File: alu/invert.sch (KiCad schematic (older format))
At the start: 16 parts

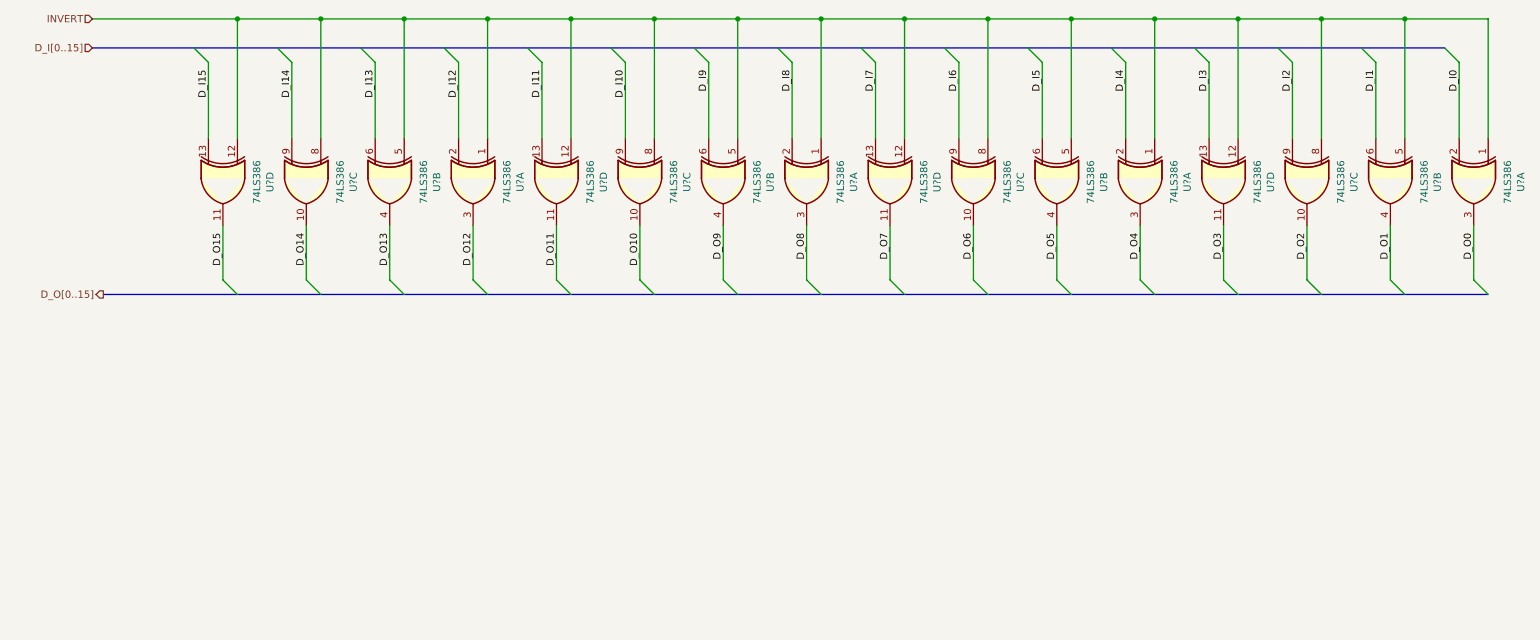
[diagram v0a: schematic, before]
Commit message: alu routed first iteration
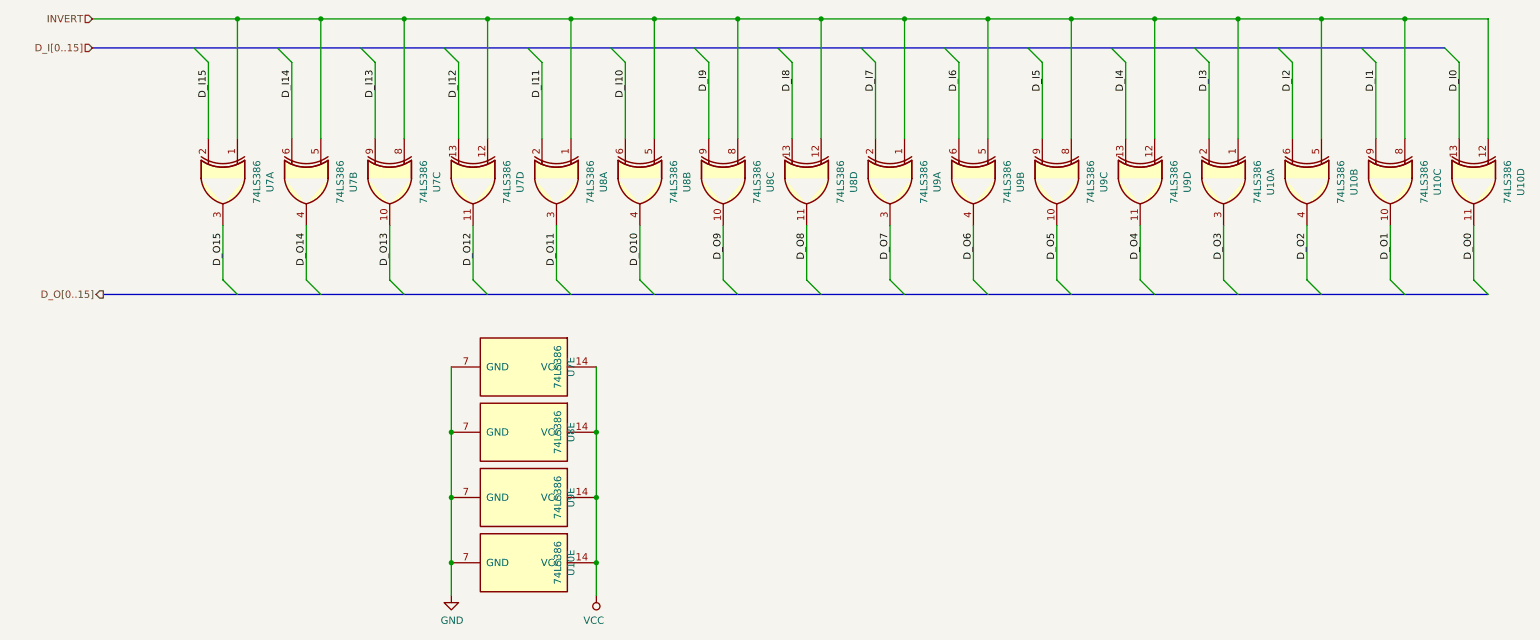
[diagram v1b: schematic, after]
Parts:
- added unit 5 of U10
- added unit 5 of U7
- added unit 5 of U8
- added unit 5 of U9
- U10, U7, U8, U9: renamed from U?; footprint (none) -> Package_DIP:DIP-14_W7.62mm_LongPads
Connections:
- net D_I0: now also U10.13; no longer U10.2
- net D_I1: now also U10.9; no longer U10.6
- net D_I10: now also U8.6; no longer U8.9
- net D_I11: now also U8.2; no longer U8.13
- net D_I12: now also U7.13; no longer U7.2
- net D_I13: now also U7.9; no longer U7.6
- net D_I14: now also U7.6; no longer U7.9
- net D_I15: now also U7.2; no longer U7.13
- net D_I2: now also U10.6; no longer U10.9
- net D_I3: now also U10.2; no longer U10.13
- net D_I4: now also U9.13; no longer U9.2
- net D_I5: now also U9.9; no longer U9.6
- net D_I6: now also U9.6; no longer U9.9
- net D_I7: now also U9.2; no longer U9.13
- net D_I8: now also U8.13; no longer U8.2
- net D_I9: now also U8.9; no longer U8.6
- net D_O0: now also U10.11; no longer U10.3
- net D_O1: now also U10.10; no longer U10.4
- net D_O10: now also U8.4; no longer U8.10
- net D_O11: now also U8.3; no longer U8.11
- net D_O12: now also U7.11; no longer U7.3
- net D_O13: now also U7.10; no longer U7.4
- net D_O14: now also U7.4; no longer U7.10
- net D_O15: now also U7.3; no longer U7.11
- net D_O2: now also U10.4; no longer U10.10
- net D_O3: now also U10.3; no longer U10.11
- net D_O4: now also U9.11; no longer U9.3
- net D_O5: now also U9.10; no longer U9.4
- net D_O6: now also U9.4; no longer U9.10
- net D_O7: now also U9.3; no longer U9.11
- net D_O8: now also U8.11; no longer U8.3
- net D_O9: now also U8.10; no longer U8.4
- net INVERT: now also U10.1, U10.12, U10.5, U10.8, U7.1, U7.12, U7.5, U7.8, U8.1, U8.12, U8.5, U8.8, U9.1, U9.12, U9.5, U9.8; no longer U10.1, U10.12, U10.5, U10.8, U7.1, U7.12, U7.5, U7.8, U8.1, U8.12, U8.5, U8.8, U9.1, U9.12, U9.5, U9.8
- new net GND: U10.7 (GND), U7.7 (GND), U8.7 (GND), U9.7 (GND)
- new net VCC: U10.14 (VCC), U7.14 (VCC), U8.14 (VCC), U9.14 (VCC)

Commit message: Commit uncomitted changes. no clue what I had done last time
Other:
- note added: "TODO replace 386 with 86"
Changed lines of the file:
@@
 $Descr A4 11693 8268
 encoding utf-8
-Sheet 7 36
+Sheet 6 36
 Title ""
 Date ""
@@
 Wire Wire Line
 	4625 3425 4625 3875
-Wire Bus Line
-	1150 1225 10475 1225
-Wire Bus Line
-	1225 2925 10775 2925
 Connection ~ 4625 3875
 Wire Wire Line
@@
 	-1   0    0    1
 $EndComp
+Wire Bus Line
+	1150 1225 10475 1225
+Wire Bus Line
+	1225 2925 10775 2925
+Text Notes 5775 3175 0    50   ~ 0
+TODO replace 386 with 86
 $EndSCHEMATC
